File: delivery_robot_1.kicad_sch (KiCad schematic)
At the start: 27 parts, among them J1 SWD, J11 IMU I2C (STEMMA QT), J12 IMU INT/RST, J2 XT30PW-M, J4 BOOT0 jumper, J5 Conn_01x03_Pin, SW1 RESET, U1 STM32F091RCTx, Y3 8MHz

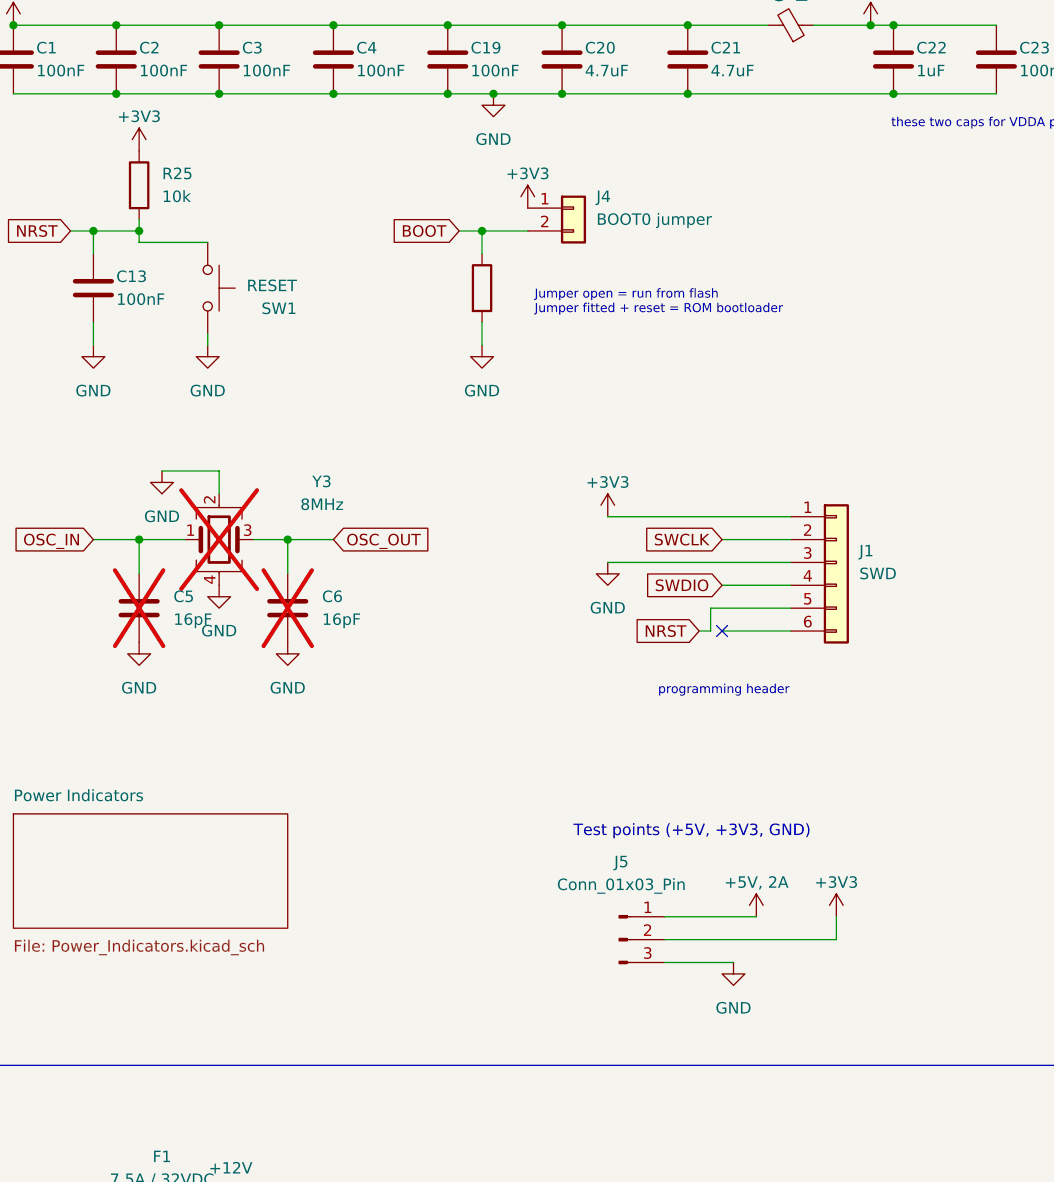
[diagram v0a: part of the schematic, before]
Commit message: Consolidate power test points into one header on a Test Points sheet
New Test_Points.kicad_sch sheet (page 10) replaces the root sheet's
3-pin J5 with a single, power-only test header:
- J5: 1x06 2.54 mm male header, ordered by voltage:
  1 GND, 2 +3V3, 3 +3.3VA, 4 +5V 2A, 5 +5V 6A AUX, 6 +12V (after F1)
- TP3: Keystone 5011 black multipurpose GND loop for a scope ground clip
+5V 6A PI stays on TP1 on the Pi 5 Interface sheet, which the Pi
bring-up steps use. The root keeps a Test Points sheet block where J5
was.

Includes manual layout edits made in KiCad: TP3 note repositioned on
the Test Points sheet, plus KiCad re-saving the Motor Control and
Power Indicators sheets (formatting only, no electrical changes).
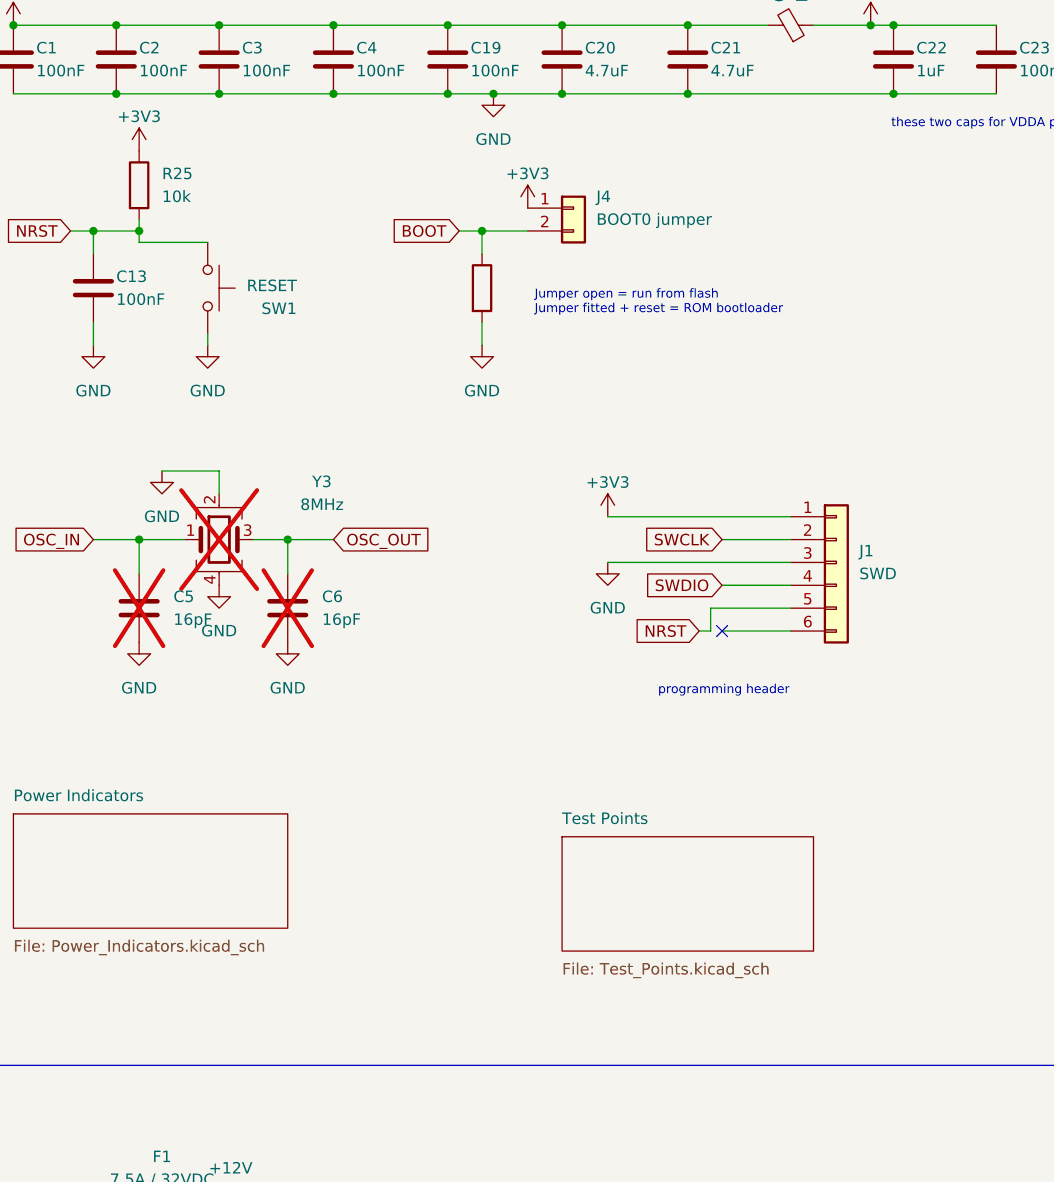
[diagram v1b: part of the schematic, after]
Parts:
- removed J5: Conn_01x03_Pin, Connector_PinHeader_2.54mm:PinHeader_1x03_P2.54mm_Vertical, symbol Connector:Conn_01x03_Pin
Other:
- added sheet Test Points (Test_Points.kicad_sch)
- note removed: "Test points (+5V, +3V3, GND)"

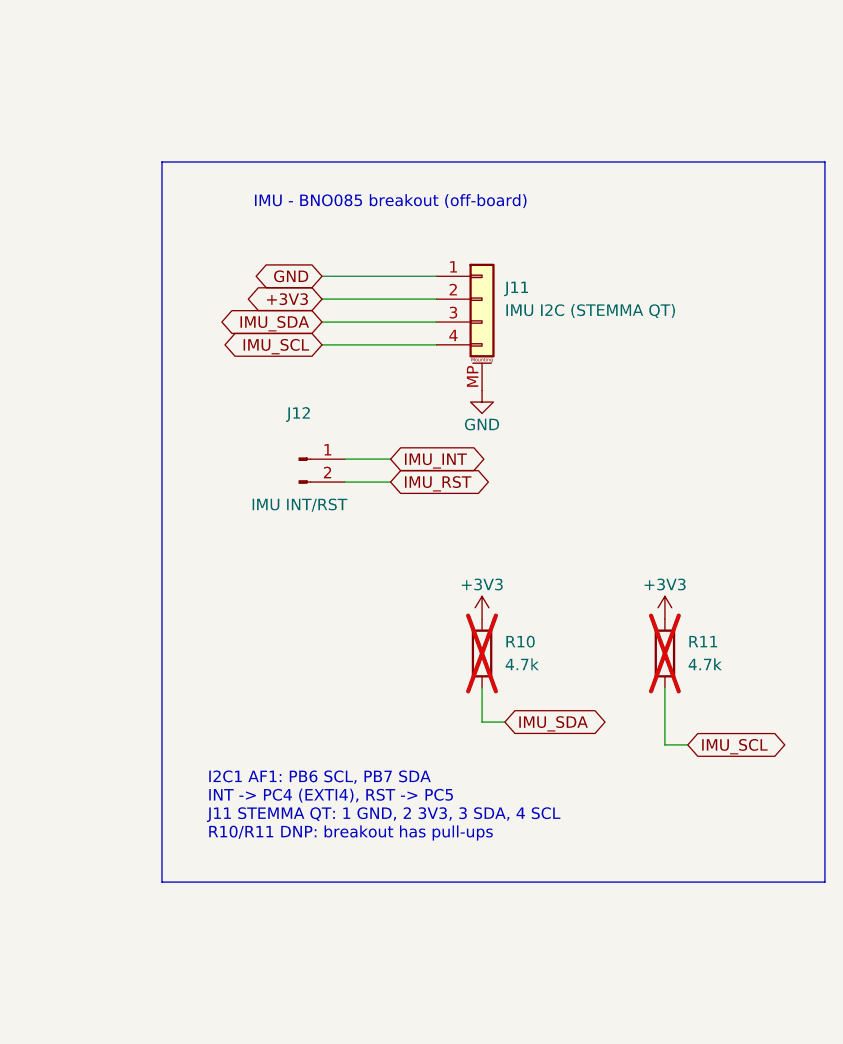
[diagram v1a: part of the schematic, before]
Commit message: Add series resistors on off-board signals and ESD arrays on J6/J7
Series protection (100R 0805, near U1, matching R12/R13 on the Pi UART)
on every off-board control and encoder line. Each line is split into
an MCU-side net and a connector-side *_CONN net:
- R26/R27 MOTOR1_PWM/DIR (J6), R28/R29 ENC1_A/B (J7)
- R30/R31 MOTOR2_PWM/DIR (J16), R32/R33 ENC2_A/B (J15)
- R34/R35 IMU_INT/RST (J12)

ESD arrays (populated) on motor 1 only, ST USBLC6-4SC6 in SOT-23-6
for hand soldering:
- U6 on J6 PWM/DIR, VBUS +3V3, C34 100 nF
- U7 on J7 encoder A/B, VBUS +5V 2A (the encoder supply), C35 100 nF
Spare channels are no-connect.

Move the IMU block (J11, J12, DNP pull-ups R10/R11) from the root
sheet to a new IMU_Interface.kicad_sch sheet (page 11) to make room for
R34/R35. It connects by global labels and has a pin note on the root
block. Update the motor pin table and the README.
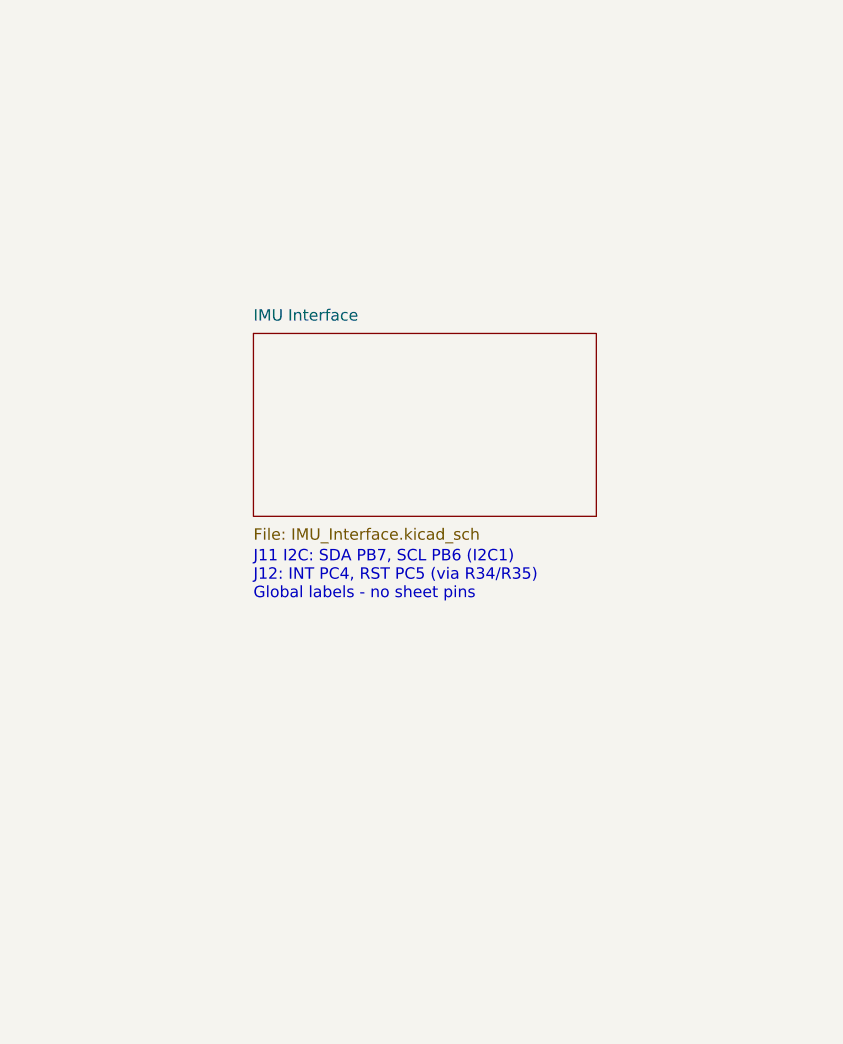
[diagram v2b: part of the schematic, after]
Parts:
- removed J11: IMU I2C (STEMMA QT), Connector_JST:JST_SH_SM04B-SRSS-TB_1x04-1MP_P1.00mm_Horizontal, symbol Connector_Generic_MountingPin:Conn_01x04_MountingPin
- removed J12: IMU INT/RST, Connector_PinHeader_2.54mm:PinHeader_1x02_P2.54mm_Vertical, symbol Connector:Conn_01x02_Pin
- removed R10, R11: 4.7k, Resistor_SMD:R_0805_2012Metric, symbol Device:R
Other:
- added sheet IMU Interface (IMU_Interface.kicad_sch)
- note added: "J11 I2C: SDA PB7, SCL PB6 (I2C1) J12: INT PC4, RST PC5 (via R34/R35) Global labels - no sheet pins"
- note removed: "I2C1 AF1: PB6 SCL, PB7 SDA INT -> PC4 (EXTI4), RST -> PC5 J11 STEMMA QT: 1 GND, 2 3V3, 3 SDA, 4 SCL R10/R11 DNP: breakout has pull-ups"
- note removed: "IMU - BNO085 breakout (off-board)"

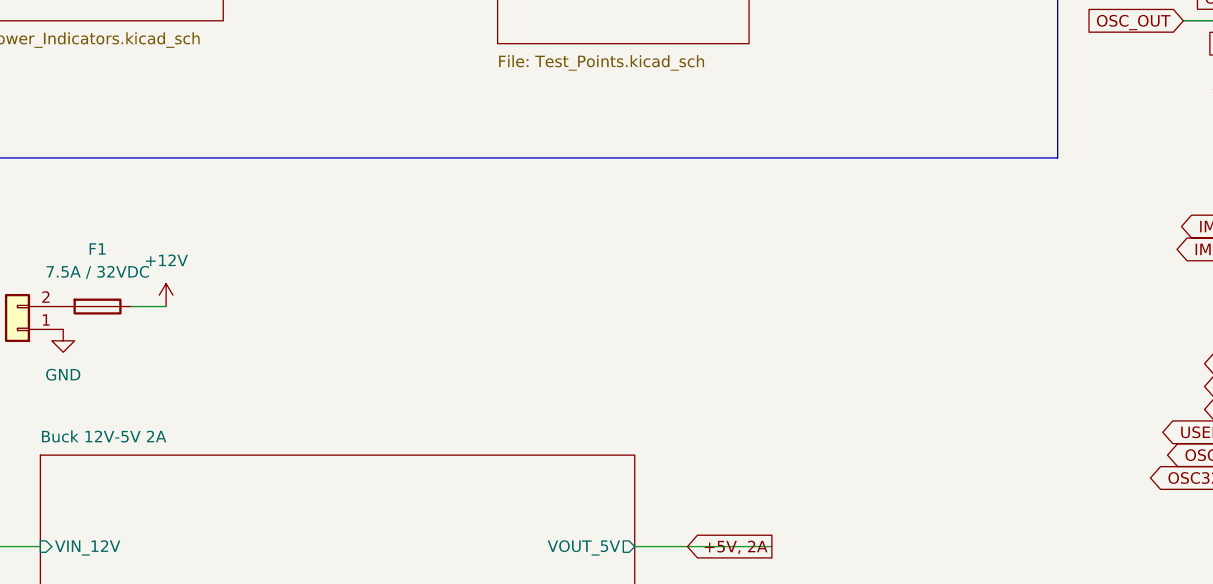
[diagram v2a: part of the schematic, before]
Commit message: Add +12V bulk capacitor, document XT30 polarity decision, use E96 values
Input (sheet 1, near J2):
- C36: 220 uF / 35 V low-ESR electrolytic (Panasonic EEU-FR1V221,
  8 x 11.5 mm radial) on +12V right after F1.
- Reverse polarity: no P-FET; rely on the keyed XT30. Note on sheet 1
  and in docs/power-supply.md: the housing cannot mate reversed, but a
  harness crimped backwards at the battery lugs is not caught (it would
  reverse-bias both bucks and C36 until F1 blows), so meter-check harness
  polarity before first power-up and after rework.

All resistor values are now E96:
- R4 40k -> 41.2k 1%: Pi rail 5.12 V (5.1 V target)
- R15 40k -> 40.2k 1%: AUX rail 5.02 V
- R8/R9 31.2k/10k -> 35.7k/11.5k: LDO 3.284 V (31.2k is E192)
- R3 510 -> 511, R21-R24 680 -> 681, R17/R10/R11 4.7k -> 4.75k
Regulator design notes, sheet notes and docs updated to match.
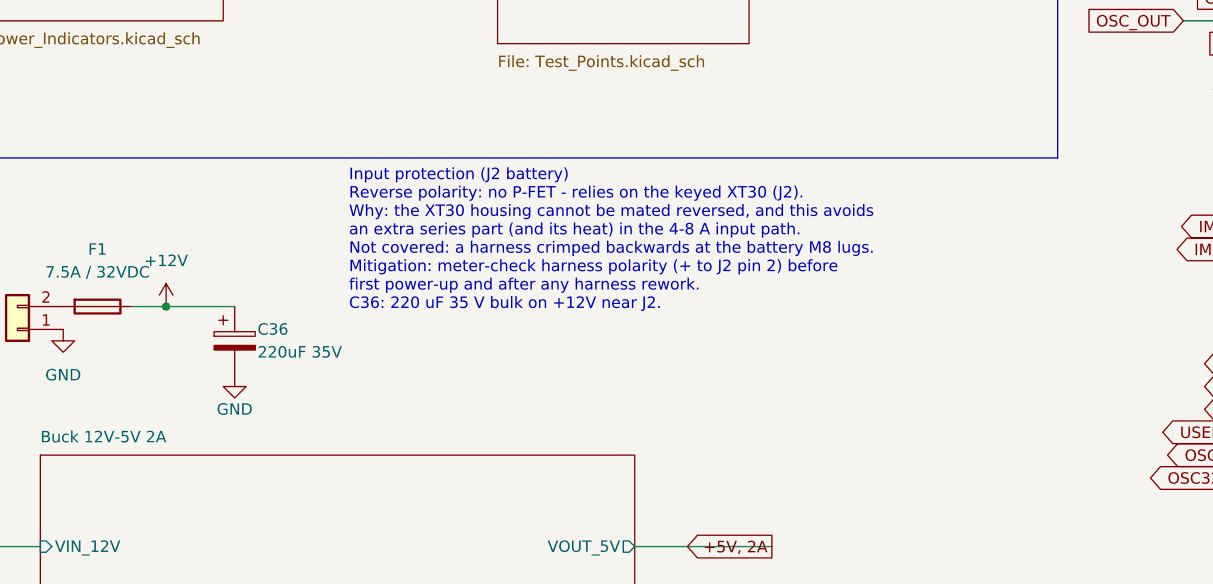
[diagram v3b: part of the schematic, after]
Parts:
- added C36: 220uF 35V, Capacitor_THT:CP_Radial_D8.0mm_P3.50mm, symbol Device:C_Polarized
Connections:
- net +12V: now also C36.1
- net GND: now also C36.2
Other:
- note added: "Input protection (J2 battery) Reverse polarity: no P-FET - relies on the keyed XT30 (J2). Why: the XT30 housing cannot be mated reversed, and this avoids an extra series part (and its heat) in the 4-8 A input path. Not covered: a harness crimped backwards at the battery M8 lugs. Mitigation: meter-check harness polarity (+ to J2 pin 2) before first power-up and after any harness rework. C36: 220 u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"
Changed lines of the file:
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@@
+		)
+	)
+	(wire
+		(pts
+			(xy 52.07 161.29) (xy 59.69 161.29)
+		)
+		(stroke
+			(width 0)
+			(type default)
+		)
+	)
+	(junction
+		(at 52.07 161.29)
+		(diameter 0)
+		(color 0 0 0 0)
+	)
+	(symbol
+		(lib_id "Device:C_Polarized")
+		(at 59.69 165.1 0)
+		(unit 1)
+		(body_style 1)
+		(exclude_from_sim no)
+		(in_bom yes)
+		(on_board yes)
+		(in_pos_files yes)
+		(dnp no)
+		(property "Reference" "C36"
+			(at 62.23 163.83 0)
+			(show_name no)
+			(do_not_autoplace no)
+			(effects
+				(font
+					(size 1.27 1.27)
+				)
+				(justify left)
+			)
+		)
+		(property "Value" "220uF 35V"
+			(at 62.23 166.37 0)
+			(show_name no)
+			(do_not_autoplace no)
+			(effects
+				(font
+					(size 1.27 1.27)
+				)
+				(justify left)
+			)
+		)
+		(property "Footprint" "Capacitor_THT:CP_Radial_D8.0mm_P3.50mm"
+			(at 59.69 165.1 0)
+			(hide yes)
+			(show_name no)
+			(do_not_autoplace no)
+			(effects
+				(font
+					(size 1.27 1.27)
+				)
+			)
+		)
+		(property "Datasheet" "https://industrial.panasonic.com/cdbs/www-data/pdf/RDF0000/ABA0000C1209.pdf"
+			(at 59.69 165.1 0)
+			(hide yes)
+			(show_name no)
+			(do_not_autoplace no)
+			(effects
+				(font
+					(size 1.27 1.27)
+				)
+			)
+		)
+		(property "Description" "+12V bulk input capacitor near J2: 220 uF / 35 V low-ESR aluminium electrolytic (950 mA ripple), 8 x 11.5 mm radial, 3.5 mm pitch. Polarized: relies on correct J2 harness polarity."
+			(at 59.69 165.1 0)
+			(hide yes)
+			(show_name no)
+			(do_not_autoplace no)
+			(effects
+				(font
+					(size 1.27 1.27)
+				)
+			)
+		)
+		(property "Manufacturer" "Panasonic"
+			(at 59.69 165.1 0)
+			(hide yes)
+			(show_name no)
+			(do_not_autoplace no)
+			(effects
+				(font
+					(size 1.27 1.27)
+				)
+			)
+		)
+		(property "MPN" "EEU-FR1V221"
+			(at 59.69 165.1 0)
+			(hide yes)
+			(show_name no)
+			(do_not_autoplace no)
+			(effects
+				(font
+					(size 1.27 1.27)
+				)
+			)
+		)
+		(pin "1"
+		)
+		(pin "2"
+		)
+		(instances
+			(project "delivery_robot_1"
+				(path "/30314d9c-15a8-4a77-8ae4-b5ba12ed5bc4"
+					(reference "C36")
+					(unit 1)
+				)
+			)
+		)
+	)
+	(symbol
+		(lib_id "power:GND")
+		(at 59.69 168.91 0)
+		(unit 1)
+		(body_style 1)
+		(exclude_from_sim no)
+		(in_bom yes)
+		(on_board yes)
+		(in_pos_files yes)
+		(dnp no)
+		(property "Reference" "#PWR0103"
+			(at 59.69 175.26 0)
+			(hide yes)
+			(show_name no)
+			(do_not_autoplace no)
+			(effects
+				(font
+					(size 1.27 1.27)
+				)
+			)
+		)
+		(property "Value" "GND"
+			(at 59.69 172.72 0)
+			(show_name no)
+			(do_not_autoplace no)
+			(effects
+				(font
+					(size 1.27 1.27)
+				)
+			)
+		)
+		(property "Footprint" ""
+			(at 59.69 168.91 0)
+			(hide yes)
+			(show_name no)
+			(do_not_autoplace no)
+			(effects
+				(font
+					(size 1.27 1.27)
+				)
+			)
+		)
+		(property "Datasheet" ""
+			(at 59.69 168.91 0)
+			(hide yes)
+			(show_name no)
+			(do_not_autoplace no)
+			(effects
+				(font
+					(size 1.27 1.27)
+				)
+			)
+		)
+		(property "Description" ""
+			(at 59.69 168.91 0)
+			(hide yes)
+			(show_name no)
+			(do_not_autoplace no)
+			(effects
+				(font
+					(size 1.27 1.27)
+				)
+			)
+		)
+		(pin "1"
+		)
+		(instances
+			(project "delivery_robot_1"
+				(path "/30314d9c-15a8-4a77-8ae4-b5ba12ed5bc4"
+					(reference "#PWR0103")
+					(unit 1)
+				)
+			)
+		)
+	)
+	(text "Input protection (J2 battery)\nReverse polarity: no P-FET - relies on the keyed XT30 (J2).\nWhy: the XT30 housing cannot be mated reversed, and this avoids\nan extra series part (and its heat) in the 4-8 A input path.\nNot covered: a harness crimped backwards at the battery M8 lugs.\nMitigation: meter-check harness polarity (+ to J2 pin 2) before\nfirst power-up and after any harness rework.\nC36: 220 uF 35 V bulk on +12V near J2."
+		(exclude_from_sim no)
+		(at 72.39 146.05 0)
+		(effects
+			(font
+				(size 1.27 1.27)
+			)
+			(justify left top)
 		)
 	)
